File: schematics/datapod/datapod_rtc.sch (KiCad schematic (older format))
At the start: 4 parts, among them J4 Conn_01x02_Female, U6 DS3231M

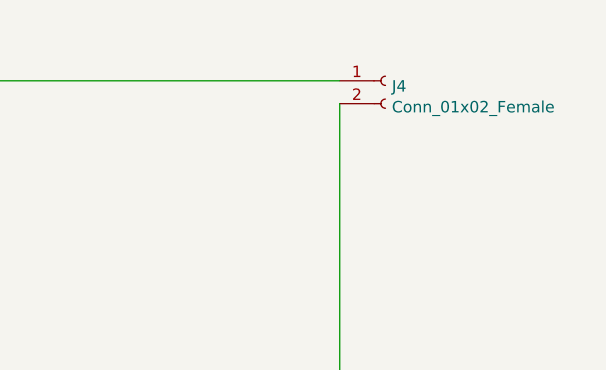
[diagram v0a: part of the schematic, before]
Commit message: added more connectors and started drawing the PCB
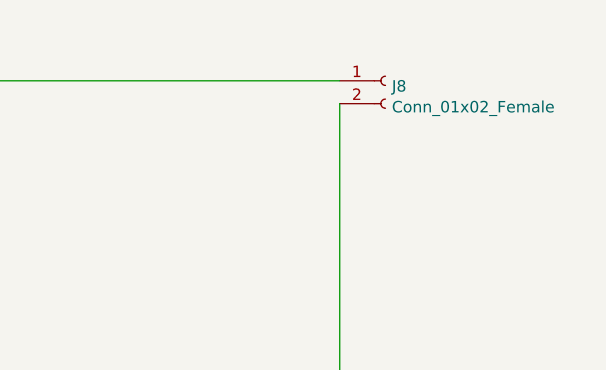
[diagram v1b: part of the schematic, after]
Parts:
- renumbered J4 to J8
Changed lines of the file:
@@
 	5000 3700 4600 3700
 $Comp
-L power:+3V3 #PWR0143
+L power:+3V3 #PWR048
 U 1 1 5E564631
 P 5400 2900
-F 0 "#PWR0143" H 5400 2750 50  0001 C CNN
+F 0 "#PWR048" H 5400 2750 50  0001 C CNN
 F 1 "+3V3" H 5415 3073 50  0000 C CNN
 F 2 "" H 5400 2900 50  0001 C CNN
@@
 	5400 2900 5400 3400
 $Comp
-L Connector:Conn_01x02_Female J4
+L Connector:Conn_01x02_Female J8
 U 1 1 5E56811E
 P 8000 2950
-F 0 "J4" H 8028 2926 50  0000 L CNN
+F 0 "J8" H 8028 2926 50  0000 L CNN
 F 1 "Conn_01x02_Female" H 8028 2835 50  0000 L CNN
 F 2 "Battery:BatteryHolder_Keystone_1058_1x2032" H 8000 2950 50  0001 C CNN
@@
 	5500 2950 7800 2950
 $Comp
-L power:GND #PWR0144
+L power:GND #PWR050
 U 1 1 5E56ABA4
 P 5500 4900
-F 0 "#PWR0144" H 5500 4650 50  0001 C CNN
+F 0 "#PWR050" H 5500 4650 50  0001 C CNN
 F 1 "GND" H 5505 4727 50  0000 C CNN
 F 2 "" H 5500 4900 50  0001 C CNN
@@
 	5500 4500 5500 4900
 $Comp
-L power:+3V3 #PWR0145
+L power:+3V3 #PWR049
 U 1 1 5E5762DB
 P 4250 4850
-F 0 "#PWR0145" H 4250 4700 50  0001 C CNN
+F 0 "#PWR049" H 4250 4700 50  0001 C CNN
 F 1 "+3V3" H 4265 5023 50  0000 C CNN
 F 2 "" H 4250 4850 50  0001 C CNN
@@
 $EndComp
 $Comp
-L power:GND #PWR0146
+L power:GND #PWR051
 U 1 1 5E57EAAC
 P 4250 6200
-F 0 "#PWR0146" H 4250 5950 50  0001 C CNN
+F 0 "#PWR051" H 4250 5950 50  0001 C CNN
 F 1 "GND" H 4255 6027 50  0000 C CNN
 F 2 "" H 4250 6200 50  0001 C CNN

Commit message: made 1st pcb
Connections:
- net GND: now also RN3.11 (R10.2)
- net VcR1: now reaches RN3.10 (R10.1)
- no-connect marks 19 -> 17
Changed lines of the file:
@@
 NoConn ~ 2600 5800
 NoConn ~ 2600 5900
-NoConn ~ 2600 6000
 NoConn ~ 3000 5600
 NoConn ~ 3000 5700
 NoConn ~ 3000 5800
 NoConn ~ 3000 5900
-NoConn ~ 3000 6000
 NoConn ~ 6000 3900
 NoConn ~ 6000 3600
@@
 NoConn ~ 3000 5500
 NoConn ~ 2600 5500
-NoConn ~ 2600 5300
 NoConn ~ 2600 5400
 Wire Wire Line
@@
 NoConn ~ 3000 5300
 NoConn ~ 3000 5400
+Text GLabel 2250 6000 0    50   Input ~ 0
+VcR1
+NoConn ~ 2600 5300
+Wire Wire Line
+	2250 6000 2600 6000
+Wire Wire Line
+	3000 6000 4250 6000
+Connection ~ 4250 6000
 $EndSCHEMATC

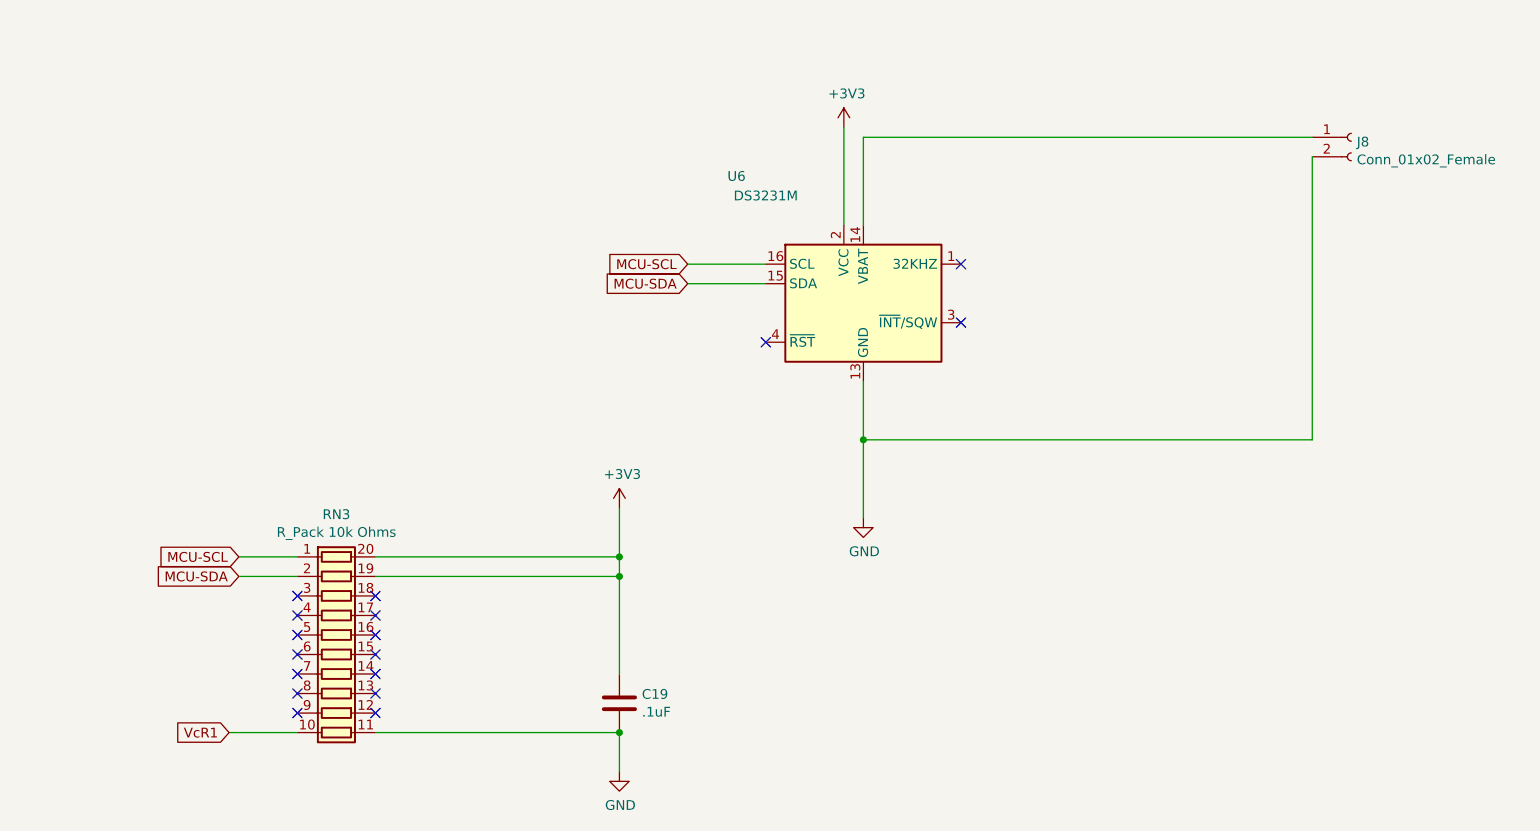
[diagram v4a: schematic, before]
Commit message: added rtc stuff , rotated db9s , added on/off transistors for max chip and sdcard
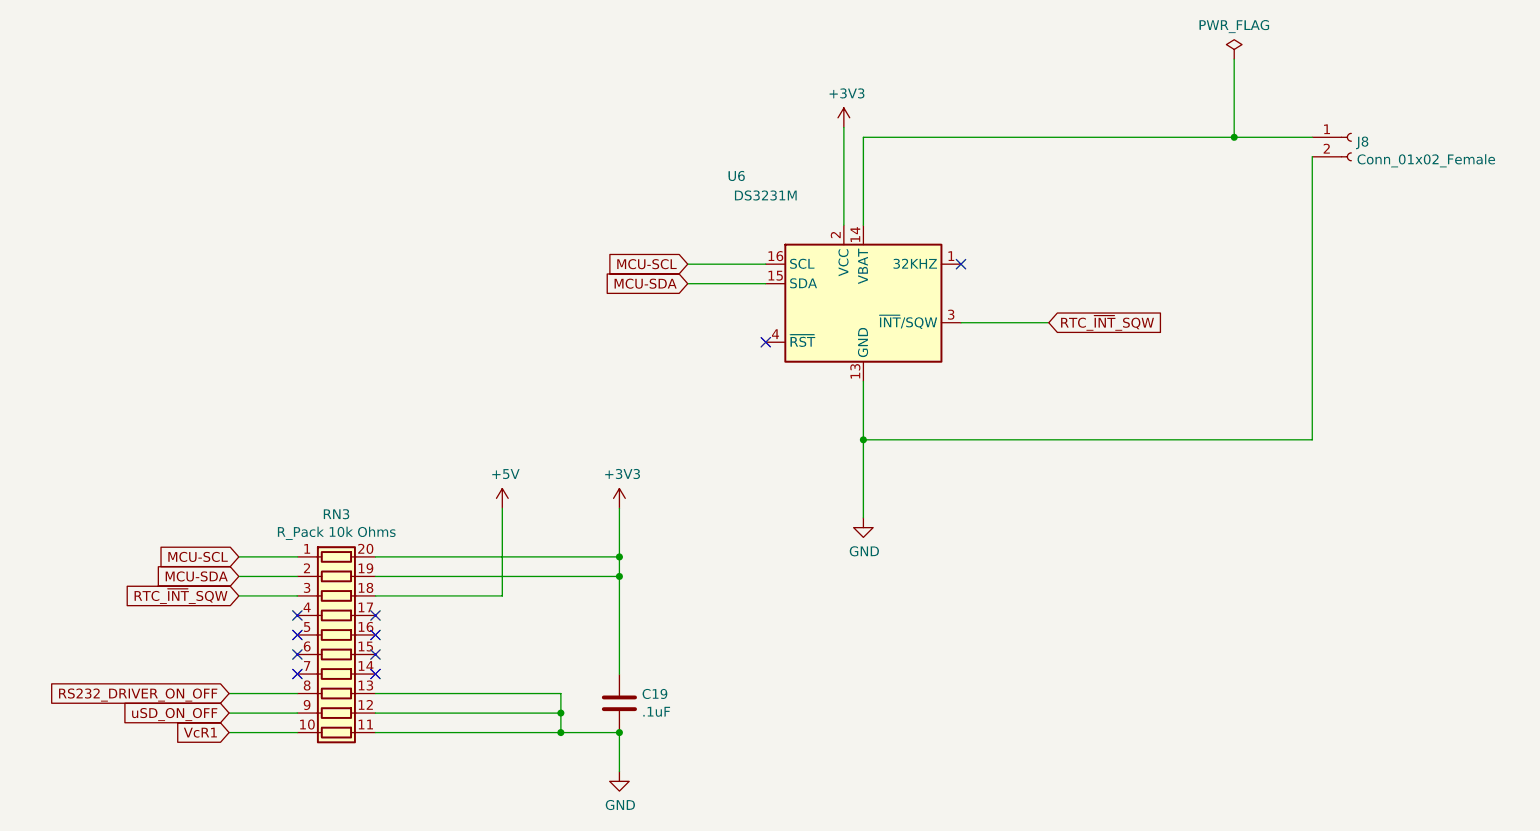
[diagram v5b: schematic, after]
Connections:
- net GND: now also RN3.12 (R9.2), RN3.13 (R8.2)
- net RTC_~INT~_SQW: now reaches U6.3 (~INT~/SQW)
- net RTC_~INT~_SQW: now also RN3.3 (R3.1)
- net +5V: now reaches RN3.18 (R3.2)
- net RS232_DRIVER_ON_OFF: now reaches RN3.8 (R8.1)
- net uSD_ON_OFF: now reaches RN3.9 (R9.1)
- no-connect marks 17 -> 10
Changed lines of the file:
@@
 	5500 2950 5500 3400
 Wire Wire Line
-	5500 2950 7800 2950
+	5500 2950 7400 2950
 $Comp
 L power:GND #PWR050
@@
 NoConn ~ 2600 5600
 NoConn ~ 2600 5700
-NoConn ~ 2600 5800
-NoConn ~ 2600 5900
 NoConn ~ 3000 5600
 NoConn ~ 3000 5700
-NoConn ~ 3000 5800
-NoConn ~ 3000 5900
-NoConn ~ 6000 3900
 NoConn ~ 6000 3600
 NoConn ~ 5000 4000
@@
 NoConn ~ 2600 5500
 NoConn ~ 2600 5400
-Wire Wire Line
-	4250 5200 4250 5700
-NoConn ~ 3000 5300
 NoConn ~ 3000 5400
 Text GLabel 2250 6000 0    50   Input ~ 0
 VcR1
-NoConn ~ 2600 5300
 Wire Wire Line
 	2250 6000 2600 6000
 Wire Wire Line
-	3000 6000 4250 6000
+	3000 6000 3950 6000
 Connection ~ 4250 6000
+Text GLabel 2300 5300 0    50   Input ~ 0
+RTC_~INT~_SQW
+Wire Wire Line
+	2300 5300 2600 5300
+Text GLabel 6450 3900 2    50   Input ~ 0
+RTC_~INT~_SQW
+Wire Wire Line
+	6000 3900 6450 3900
+$Comp
+L power:+5V #PWR05
+U 1 1 5E1F51D4
+P 3650 4850
+F 0 "#PWR05" H 3650 4700 50  0001 C CNN
+F 1 "+5V" H 3665 5023 50  0000 C CNN
+F 2 "" H 3650 4850 50  0001 C CNN
+F 3 "" H 3650 4850 50  0001 C CNN
+	1    3650 4850
+	1    0    0    -1
+$EndComp
+Wire Wire Line
+	4250 5200 4250 5700
+Wire Wire Line
+	3000 5300 3650 5300
+Wire Wire Line
+	3650 5300 3650 4850
+Text GLabel 2250 5800 0    50   Input ~ 0
+RS232_DRIVER_ON_OFF
+Wire Wire Line
+	2600 5900 2250 5900
+Wire Wire Line
+	3000 5900 3950 5900
+Wire Wire Line
+	3950 5900 3950 6000
+Connection ~ 3950 6000
+Wire Wire Line
+	3950 6000 4250 6000
+Text GLabel 2250 5900 0    50   Input ~ 0
+uSD_ON_OFF
+Wire Wire Line
+	2600 5800 2250 5800
+Wire Wire Line
+	3000 5800 3950 5800
+Wire Wire Line
+	3950 5800 3950 5900
+Connection ~ 3950 5900
+$Comp
+L power:PWR_FLAG #FLG0109
+U 1 1 5E2CFE5E
+P 7400 2550
+F 0 "#FLG0109" H 7400 2625 50  0001 C CNN
+F 1 "PWR_FLAG" H 7400 2723 50  0000 C CNN
+F 2 "" H 7400 2550 50  0001 C CNN
+F 3 "~" H 7400 2550 50  0001 C CNN
+	1    7400 2550
+	1    0    0    -1
+$EndComp
+Wire Wire Line
+	7400 2550 7400 2950
+Connection ~ 7400 2950
+Wire Wire Line
+	7400 2950 7800 2950
 $EndSCHEMATC
